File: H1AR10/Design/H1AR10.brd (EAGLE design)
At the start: 34.6 x 30 mm, 42 parts, among them P1 HEXABIT_17.32_NO_P3, U1 STM32F091CBU6, U2 FT230XQ, U3 TI_NATIONAL_SEMICONDUCTOR_LM3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, X1 XTALL_CSTCE8M00G52, X3 USB-B-H

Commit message: final un-checked
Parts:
- removed JP1: (no value), Hexabitz:JP1
- removed U3: TI_NATIONAL_SEMICONDUCTOR_LM3940IMP-3.3TI_NATIONAL_SEMICOND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, TI National Semiconductor - LM3940IMP-3.3:TI_NATIONAL_SEMICONDUCTOR_LM3940IMP-3.3_2
- added PWR: 3-644456-2, Hexabitz:TE_3-644456-2
- added U4: FT230XQ-R, Hexabitz:QFN16
- C16: device Hexabitz:C3225 -> Hexabitz:C-3225
- D1, D2, D3: value VLMS1300-GS08 -> RED
- U2: value FT230XQ -> LM3940IMP-3.3; device Hexabitz:QFN16 -> Hexabitz:SOT230P696X180-4N
- moved U2 16.4 mm to (35.3, 41.0), flipped to the top, turned to 0 degrees
- moved B 11.2 mm to (47.5, 35.6), turned to 180 degrees
- moved R 6.74 mm to (47.5, 38.1), turned to 180 degrees
- moved R9 4.86 mm to (41.7, 25.8), turned to 0 degrees
- moved C3 4.54 mm to (25.4, 43.7), turned to 270 degrees
- moved C17 4.07 mm to (26.9, 40.4), turned to 270 degrees
- moved R6 3.98 mm to (41.7, 25.1)
- moved FB2 3.74 mm to (30.2, 43.3), turned to 270 degrees
- moved R5 3.73 mm to (29.3, 25.7), turned to 0 degrees
- moved C7 3.42 mm to (39.5, 44.2), turned to 270 degrees
- moved C1 3.23 mm to (43.5, 44.9)
- moved X1 3.08 mm to (41.9, 42.1), turned to 0 degrees
- moved R3 2.45 mm to (40.9, 37.9), flipped to the top, turned to 90 degrees
- moved C8 2.38 mm to (30.0, 38.5), turned to 270 degrees
- moved C16 2.10 mm to (29.8, 39.4), turned to 90 degrees
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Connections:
- removed net VDD2: C15.1, U2.8, U2.9
- net GND: now also U1.P$2, U2.2, U2.4, U4.13, U4.17, U4.3; no longer U1.P$26, U1.P$43, U2.13, U2.3, U2.EXP, U3.2, U3.4
- net N$10: now also U4.11; no longer U2.11
- net N$11: now also U4.7; no longer U2.7
- net N$12: now also U4.6; no longer U2.6
- net N$15: now also PWR.1; no longer JP1.2
- net N$16: now also U2.1; no longer U3.1
- net N$17: now also PWR.2; no longer JP1.1
- net N$3: now also U4.5; no longer U2.5
- net UART1_CTS: now also U4.4; no longer U2.4
- net UART1_RTS: now also U4.16; no longer U2.16
- net UART1_RX: now also U4.15; no longer U2.15
- net UART1_TX: now also U4.2; no longer U2.2
- net VBUS_SENSE: now also U4.14; no longer U2.14
- net VDD: now also C15.1, U2.3, U4.1, U4.10, U4.8, U4.9; no longer U2.1, U2.10, U3.3
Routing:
- net GND: track 38.0 -> 20.4 mm, vias 3 -> 6
- net R1: track 6.22 -> 18.0 mm, vias 0 -> 2
- net B1: track 13.1 -> 23.6 mm, vias 1 -> 2
- net N$15: track 36.1 -> 26.2 mm
- net N$13: track 8.56 -> 15.5 mm
- net UART6_RX: track 17.7 -> 23.0 mm
- net VBUS_SENSE: track 8.28 -> 11.9 mm
- net VDD2: track 3.48 -> 0.00 mm
- net UART2_TX: track 17.0 -> 19.9 mm
- net VDDA: track 8.91 -> 11.7 mm
- net VDD: track 34.6 -> 37.4 mm, vias 5 -> 6
- net N$9: track 3.45 -> 5.86 mm, vias 0 -> 1
- net UART4_TX: track 28.0 -> 30.0 mm
- net N$10: track 10.3 -> 8.31 mm
- net N$12: track 4.75 -> 2.80 mm
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- added copper zone on layer 1, net GND
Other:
- board text added: "D"

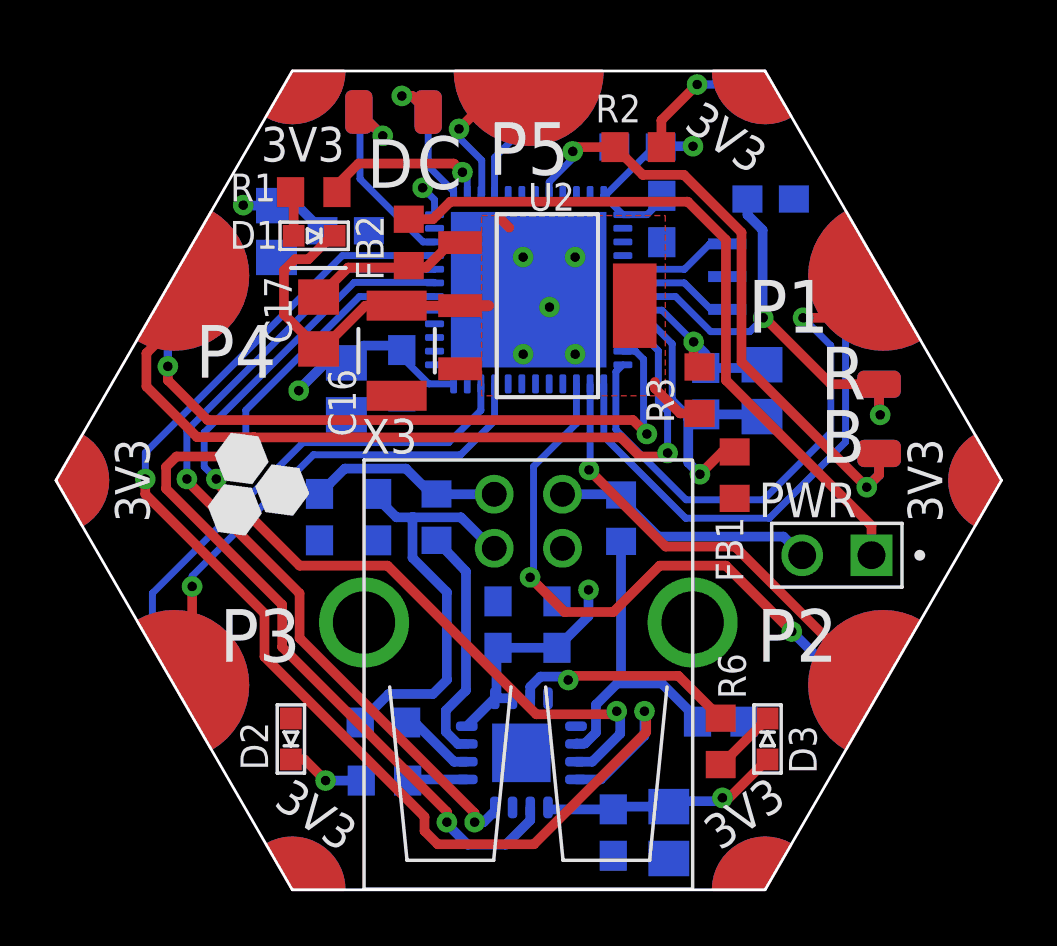
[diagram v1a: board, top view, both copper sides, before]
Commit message: rotate "C" & "D" pads 90 degrees chage X2 (label) to PUSB* change the led pin to (PB1) pin make "R" pad away enough form "B" pad fix some clearnce  issues
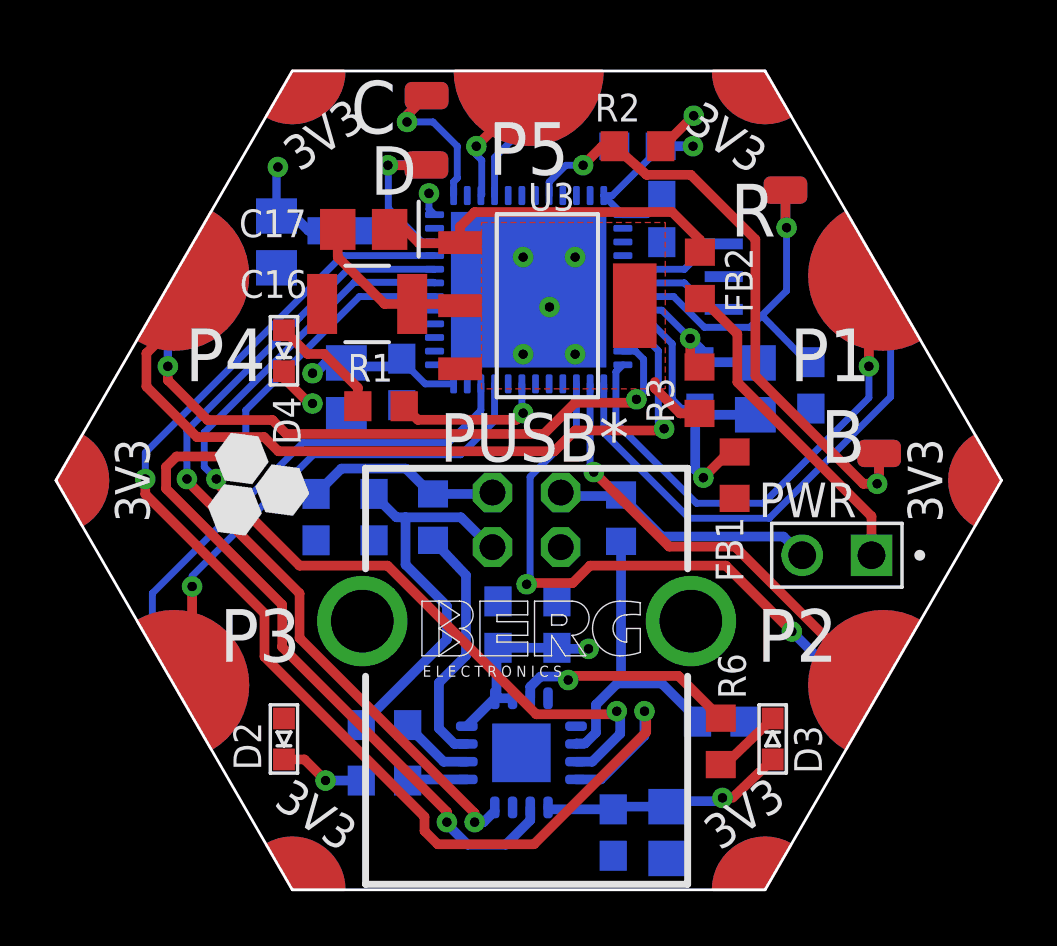
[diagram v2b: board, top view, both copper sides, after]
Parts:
- removed D1: RED, Hexabitz:VLMS1300-GS08
- removed U4: FT230XQ-R, Hexabitz:QFN16
- removed X3: USB-B-H, Hexabitz:USB-B-H
- added D4: RED, Hexabitz:VLMS1300-GS08
- added PUSB*: USB-B, Hexabitz:PN61729-S
- added U3: LM3940IMP-3.3, Hexabitz:SOT230P696X180-4N
- D3: value RED -> Green
- U2: value LM3940IMP-3.3 -> FT230XQ-R; device Hexabitz:SOT230P696X180-4N -> Hexabitz:QFN16
- moved U2 16.4 mm to (34.4, 24.6), flipped to the bottom, turned to 90 degrees
- moved FB2 10.7 mm to (40.9, 42.1), turned to 90 degrees
- moved R1 8.22 mm to (29.2, 37.3)
- moved R 7.90 mm to (44.0, 45.3)
- moved C1 6.99 mm to (45.0, 38.1), turned to 270 degrees
- moved C17 3.81 mm to (28.6, 43.8), turned to 180 degrees
- moved D 3.15 mm to (30.9, 46.2), turned to 0 degrees
- moved C16 2.03 mm to (28.7, 41.1), turned to 0 degrees
- moved C 0.61 mm to (30.9, 48.7), turned to 180 degrees
- moved C3 0.38 mm to (25.4, 43.4)
- moved C8 0.32 mm to (30.0, 38.2)
- moved C5 0.30 mm to (40.9, 38.1)
- moved D2 0.25 mm to (25.7, 25.1)
- moved C2 0.25 mm to (42.9, 38.0)
- moved D3 0.19 mm to (43.6, 25.1)
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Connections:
- removed net N$1: R1.2, U1.P$38
- removed net N$4: D1.A, R1.1
- new net N$18: D4.A, R1.1
- new net N$19: R1.2, U1.P$19
- net GND: now also D4.C, PUSB*.4, PUSB*.S1, PUSB*.S2, U2.13, U2.17, U2.3, U3.2, U3.4; no longer D1.C, U2.2, U2.4, U4.13, U4.17, U4.3, X3.GND
- net N$10: now also U2.11; no longer U4.11
- net N$11: now also U2.7; no longer U4.7
- net N$12: now also U2.6; no longer U4.6
- net N$13: now also PUSB*.3; no longer X3.D+
- net N$14: now also PUSB*.2; no longer X3.D-
- net N$16: now also U3.1; no longer U2.1
- net N$17: now also PUSB*.1; no longer X3.VBUS
- net N$3: now also U2.5; no longer U4.5
- net UART1_CTS: now also U2.4; no longer U4.4
- net UART1_RTS: now also U2.16; no longer U4.16
- net UART1_RX: now also U2.15; no longer U4.15
- net UART1_TX: now also U2.2; no longer U4.2
- net VBUS_SENSE: now also U2.14; no longer U4.14
- net VDD: now also U2.1, U2.10, U2.8, U2.9, U3.3; no longer U2.3, U4.1, U4.10, U4.8, U4.9
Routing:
- net N$15: track 26.2 -> 12.1 mm
- net GND: track 20.4 -> 11.9 mm, vias 6 -> 7
- net N$16: track 6.64 -> 13.3 mm
- net N$1: track 6.24 -> 0.00 mm, vias 1 -> 0
- net N$19: track 0.00 -> 5.76 mm, vias 0 -> 1
- net N$18: track 0.00 -> 4.25 mm
- net R1: track 18.0 -> 14.6 mm, vias 2 -> 1
- net VDD: track 37.4 -> 34.0 mm
- net N$7: track 8.64 -> 6.63 mm
- net N$4: track 1.65 -> 0.00 mm
- net UART2_TX: track 19.9 -> 18.5 mm
- net UART5_TX: track 5.95 -> 4.76 mm
- net UART4_RX: track 25.9 -> 24.8 mm
- net UART4_TX: track 30.0 -> 29.2 mm
- net N$13: track 15.5 -> 14.8 mm
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
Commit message: no message
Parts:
- renumbered D4 to D1
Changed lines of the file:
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@@
 <grid distance="5" unitdist="mil" unit="mil" style="lines" multiple="1" display="yes" altdistance="5" altunitdist="mil" altunit="mil"/>
 <layers>
-<layer number="1" name="Top" color="4" fill="1" visible="no" active="yes"/>
+<layer number="1" name="Top" color="4" fill="1" visible="yes" active="yes"/>
 <layer number="2" name="Route2" color="16" fill="1" visible="no" active="no"/>
-<layer number="3" name="Route3" color="4" fill="3" visible="no" active="yes"/>
-<layer number="4" name="Route4" color="1" fill="4" visible="no" active="yes"/>
-<layer number="5" name="Route5" color="4" fill="4" visible="no" active="yes"/>
-<layer number="6" name="Route6" color="1" fill="8" visible="no" active="yes"/>
-<layer number="7" name="Route7" color="4" fill="8" visible="no" active="yes"/>
-<layer number="8" name="Route8" color="1" fill="2" visible="no" active="yes"/>
-<layer number="9" name="Route9" color="4" fill="2" visible="no" active="yes"/>
-<layer number="10" name="Route10" color="1" fill="7" visible="no" active="yes"/>
-<layer number="11" name="Route11" color="4" fill="7" visible="no" active="yes"/>
-<layer number="12" name="Route12" color="1" fill="5" visible="no" active="yes"/>
-<layer number="13" name="Route13" color="4" fill="5" visible="no" active="yes"/>
-<layer number="14" name="Route14" color="1" fill="6" visible="no" active="yes"/>
+<layer number="3" name="Route3" color="4" fill="3" visible="yes" active="yes"/>
+<layer number="4" name="Route4" color="1" fill="4" visible="yes" active="yes"/>
+<layer number="5" name="Route5" color="4" fill="4" visible="yes" active="yes"/>
+<layer number="6" name="Route6" color="1" fill="8" visible="yes" active="yes"/>
+<layer number="7" name="Route7" color="4" fill="8" visible="yes" active="yes"/>
+<layer number="8" name="Route8" color="1" fill="2" visible="yes" active="yes"/>
+<layer number="9" name="Route9" color="4" fill="2" visible="yes" active="yes"/>
+<layer number="10" name="Route10" color="1" fill="7" visible="yes" active="yes"/>
+<layer number="11" name="Route11" color="4" fill="7" visible="yes" active="yes"/>
+<layer number="12" name="Route12" color="1" fill="5" visible="yes" active="yes"/>
+<layer number="13" name="Route13" color="4" fill="5" visible="yes" active="yes"/>
+<layer number="14" name="Route14" color="1" fill="6" visible="yes" active="yes"/>
 <layer number="15" name="Route15" color="23" fill="1" visible="no" active="no"/>
 <layer number="16" name="Bottom" color="1" fill="1" visible="yes" active="yes"/>
@@
 <layer number="19" name="Unrouted" color="6" fill="1" visible="yes" active="yes"/>
 <layer number="20" name="Dimension" color="24" fill="1" visible="yes" active="yes"/>
-<layer number="21" name="tPlace" color="12" fill="1" visible="no" active="yes"/>
+<layer number="21" name="tPlace" color="12" fill="1" visible="yes" active="yes"/>
 <layer number="22" name="bPlace" color="9" fill="1" visible="yes" active="yes"/>
-<layer number="23" name="tOrigins" color="15" fill="1" visible="no" active="yes"/>
+<layer number="23" name="tOrigins" color="15" fill="1" visible="yes" active="yes"/>
 <layer number="24" name="bOrigins" color="15" fill="1" visible="yes" active="yes"/>
-<layer number="25" name="tNames" color="12" fill="1" visible="no" active="yes"/>
+<layer number="25" name="tNames" color="12" fill="1" visible="yes" active="yes"/>
 <layer number="26" name="bNames" color="9" fill="1" visible="yes" active="yes"/>
 <layer number="27" name="tValues" color="7" fill="1" visible="no" active="yes"/>
@@
 <layer number="37" name="tTest" color="7" fill="1" visible="no" active="yes"/>
 <layer number="38" name="bTest" color="7" fill="1" visible="no" active="yes"/>
-<layer number="39" name="tKeepout" color="4" fill="11" visible="no" active="yes"/>
+<layer number="39" name="tKeepout" color="4" fill="11" visible="yes" active="yes"/>
 <layer number="40" name="bKeepout" color="1" fill="11" visible="yes" active="yes"/>
-<layer number="41" name="tRestrict" color="4" fill="10" visible="no" active="yes"/>
+<layer number="41" name="tRestrict" color="4" fill="10" visible="yes" active="yes"/>
 <layer number="42" name="bRestrict" color="1" fill="10" visible="yes" active="yes"/>
 <layer number="43" name="vRestrict" color="2" fill="10" visible="no" active="yes"/>
@@
 <layer number="49" name="Reference" color="7" fill="1" visible="no" active="yes"/>
 <layer number="50" name="dxf" color="7" fill="1" visible="no" active="no"/>
-<layer number="51" name="tDocu" color="7" fill="1" visible="no" active="yes"/>
+<layer number="51" name="tDocu" color="7" fill="1" visible="yes" active="yes"/>
 <layer number="52" name="bDocu" color="7" fill="1" visible="yes" active="yes"/>
 <layer number="53" name="tGND_GNDA" color="7" fill="9" visible="no" active="no"/>
@@
 <attribute name="VALUE" x="27.672028125" y="35.447984375" size="1.016" layer="27"/>
 </element>
-<element name="D4" library="Hexabitz" package="VLMS1300-GS08" value="RED" x="25.654" y="39.37" smashed="yes">
+<element name="D1" library="Hexabitz" package="VLMS1300-GS08" value="RED" x="25.654" y="39.37" smashed="yes">
 <attribute name="MFN" value="Vishay" x="19.558" y="40.767" size="1.778" layer="27" display="off"/>
 <attribute name="MPN" value="VLMS1300-GS08" x="19.558" y="40.767" size="1.778" layer="27" display="off"/>
@@
 <contactref element="PUSB*" pad="S1"/>
 <contactref element="PUSB*" pad="S2"/>
-<contactref element="D4" pad="C"/>
+<contactref element="D1" pad="C"/>
 <via x="26.69971875" y="37.43528125" extent="1-16" drill="0.35"/>
 <wire x1="30.352" y1="41.0845" x2="32.0421" y2="41.0845" width="0.3556" layer="1"/>
@@
 <signal name="N$18">
 <contactref element="R1" pad="1"/>
-<contactref element="D4" pad="A"/>
+<contactref element="D1" pad="A"/>
 <wire x1="25.654" y1="40.12" x2="26.5211" y2="39.2529" width="0.3556" layer="1"/>
 <wire x1="26.5211" y1="39.2529" x2="27.12218125" y2="39.2529" width="0.3556" layer="1"/>

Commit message: no message
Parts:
- D2: value RED -> YELLOW
- D3: value Green -> ORANGE
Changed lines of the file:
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@@
 <attribute name="VOLTAGE_RATING" value="50" x="26.82875" y="33.274" size="1.778" layer="28" rot="MR270" display="off"/>
 </element>
-<element name="D3" library="Hexabitz" package="VLMS1300-GS08" value="Green" x="43.561" y="25.146" smashed="yes" rot="R180">
+<element name="D3" library="Hexabitz" package="VLMS1300-GS08" value="ORANGE" x="43.561" y="25.146" smashed="yes" rot="R180">
 <attribute name="MFN" value="Vishay" x="49.657" y="18.669" size="1.778" layer="27" rot="R180" display="off"/>
-<attribute name="MPN" value="VLMTG1300-GS08 " x="49.657" y="18.669" size="1.778" layer="27" rot="R180" display="off"/>
+<attribute name="MPN" value="VLMO1300-GS08
+" x="49.657" y="18.669" size="1.778" layer="27" rot="R180" display="off"/>
 <attribute name="NAME" x="45.363" y="23.87625" size="1.016" layer="25" rot="R90"/>
-<attribute name="OCTOPART_URL" value="https://octopart.com/vlmtg1300-gs08-vishay-21709202" x="49.657" y="18.669" size="1.778" layer="27" rot="R180" display="off"/>
+<attribute name="OCTOPART_URL" value="https://octopart.com/vlmo1300-gs08-vishay-21709200?r=sp#" x="49.657" y="18.669" size="1.778" layer="27" rot="R180" display="off"/>
 <attribute name="VALUE" value="RED" x="45.561" y="28.021" size="1.016" layer="27" rot="R180"/>
 </element>
-<element name="D2" library="Hexabitz" package="VLMS1300-GS08" value="RED" x="25.654" y="25.146" smashed="yes">
+<element name="D2" library="Hexabitz" package="VLMS1300-GS08" value="YELLOW" x="25.654" y="25.146" smashed="yes">
 <attribute name="MFN" value="Vishay" x="19.558" y="31.496" size="1.778" layer="27" display="off"/>
-<attribute name="MPN" value="VLMS1300-GS08" x="19.558" y="31.496" size="1.778" layer="27" display="off"/>
+<attribute name="MPN" value="VLMY1300-GS08" x="19.558" y="31.496" size="1.778" layer="27" display="off"/>
 <attribute name="NAME" x="24.82075" y="24.00325" size="1.016" layer="25" rot="R90"/>
-<attribute name="OCTOPART_URL" value="https://octopart.com/vlms1300-gs08-vishay-21709201" x="19.558" y="31.496" size="1.778" layer="27" display="off"/>
+<attribute name="OCTOPART_URL" value="https://octopart.com/vlmy1300-gs08-vishay-21709204?r=sp" x="19.558" y="31.496" size="1.778" layer="27" display="off"/>
 <attribute name="VALUE" value="RED" x="23.654" y="22.271" size="1.016" layer="27"/>
 </element>
